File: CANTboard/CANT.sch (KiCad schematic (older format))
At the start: 24 parts, among them P1 SWD, P2 CAN, P3 USB, U1 STM32F042C6T6, U2 MCP2562-E/SN, U3 LD1117S33TR, U4 74LVC1G66

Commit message: Laid out CANT board based on STM32H7
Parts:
- removed C5, C6: 0.1uF, Capacitors_SMD:C_0805_HandSoldering, symbol pspice:C
- removed C7: 100nF, Capacitors_SMD:C_0805_HandSoldering, symbol pspice:C
- removed C8: 10uF, Capacitors_SMD:C_0805_HandSoldering, symbol pspice:C
- removed P2: CAN, Connectors_JST:JST_XH_S04B-XH-A_04x2.50mm_Angled, symbol Connector:Screw_Terminal_01x04
- removed U1: STM32F042C6T6, Housings_QFP:LQFP-48_7x7mm_Pitch0.5mm, symbol CANT-rescue:STM32F042C6T6-YaCANi
- removed U2: MCP2562-E/SN, Housings_SOIC:SOIC-8_3.9x4.9mm_Pitch1.27mm, symbol Interface_CAN_LIN:MCP2562-E-SN
- added C10, C9: 2.2uF, Capacitor_SMD:C_0805_2012Metric, symbol Device:C
- added C11, C12, C13: 100nF, Capacitor_SMD:C_0805_2012Metric, symbol pspice:C
- added C14: 100nF, Capacitor_SMD:C_0805_2012Metric, symbol Device:C_Small
- added C15: 1uF, Capacitor_SMD:C_0805_2012Metric, symbol Device:C_Small
- added C16, C17, C5, C6, C7: 100nF, Capacitor_SMD:C_0805_2012Metric, symbol Device:C
- added C8: 10uF, Capacitor_SMD:C_0805_2012Metric, symbol Device:C
- added D3: LED-RED, LED_SMD:LED_0805_2012Metric, symbol Device:LED
- added J1: Screw_Terminal_01x04, Connector_PinHeader_2.54mm:PinHeader_1x04_P2.54mm_Horizontal, symbol Connector:Screw_Terminal_01x04
- added JP3: Jumper_NC_Dual, Connector_PinHeader_2.54mm:PinHeader_1x03_P2.54mm_Vertical, symbol Device:Jumper_NC_Dual
- added R5, R7: 4.7K, Resistor_SMD:R_0805_2012Metric, symbol pspice:R
- added R6: 120, Resistor_SMD:R_0805_2012Metric, symbol pspice:R
- added R8: 68, Resistor_SMD:R_0805_2012Metric, symbol pspice:R
- added U1: STM32H743VITx, Package_QFP:LQFP-100_14x14mm_P0.5mm, symbol MCU_ST_STM32H7:STM32H743VITx
- added U2, U6: MCP2558FD-xSN, Package_SO:SOIC-8_3.9x4.9mm_P1.27mm, symbol Interface_CAN_LIN:MCP2558FD-xSN
- added U5: 74LVC1G66, Package_TO_SOT_SMD:SOT-353_SC-70-5_Handsoldering, symbol 74xGxx:74LVC1G66
- C1, C2, C4: value 0.1uF -> 100nF; footprint Capacitors_SMD:C_0805_HandSoldering -> Capacitor_SMD:C_0805_2012Metric
- C3: value 1uF -> 4.7uF; footprint Capacitors_SMD:C_0805_HandSoldering -> Capacitor_SMD:C_0805_2012Metric
- F1: footprint Capacitors_SMD:C_0805_HandSoldering -> Capacitor_SMD:C_0805_2012Metric
- JP1, JP2: footprint Pin_Headers:Pin_Header_Straight_1x03_Pitch2.54mm -> Connector_PinHeader_2.54mm:PinHeader_1x03_P2.54mm_Vertical
- P1: footprint Pin_Headers:Pin_Header_Straight_1x05_Pitch2.54mm -> Connector_PinHeader_2.54mm:PinHeader_1x05_P2.54mm_Vertical
- P3: footprint Connectors_Molex:USB_Micro-B_Molex_47346-0001 -> Connector_USB:USB_Micro-B_Molex_47346-0001
- R1, R2: footprint Resistors_SMD:R_0805_HandSoldering -> Resistor_SMD:R_0805_2012Metric
- R3, R4: value R -> 68; footprint Resistors_SMD:R_0805_HandSoldering -> Resistor_SMD:R_0805_2012Metric
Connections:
- net labels added: CAN1_H, CAN1_L, CAN1_RX, CAN1_SHORT, CAN1_TX, CAN2_H, CAN2_L, CAN2_RX, CAN2_SHORT, CAN2_TX, LED_ACT1, LED_ACT2, LED_PWR1
- net labels removed: CAN_H, CAN_L, CAN_RX, CAN_SHORT, CAN_TX, LED_ACT, LED_PWR
- wire segments 54 -> 86
- no-connect marks 32 -> 73
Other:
- moved on the sheet: C1, C2, C3, C4, D1, D2, F1, JP1, JP2, P1, P3, R1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

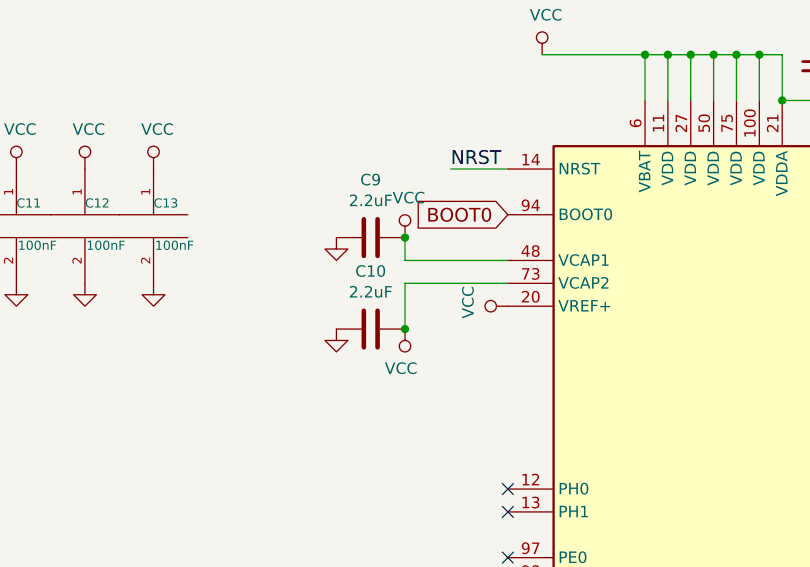
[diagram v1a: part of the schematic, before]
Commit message: Fix VCAP connection issue - apparently, these are not supposed to be connected to VDD
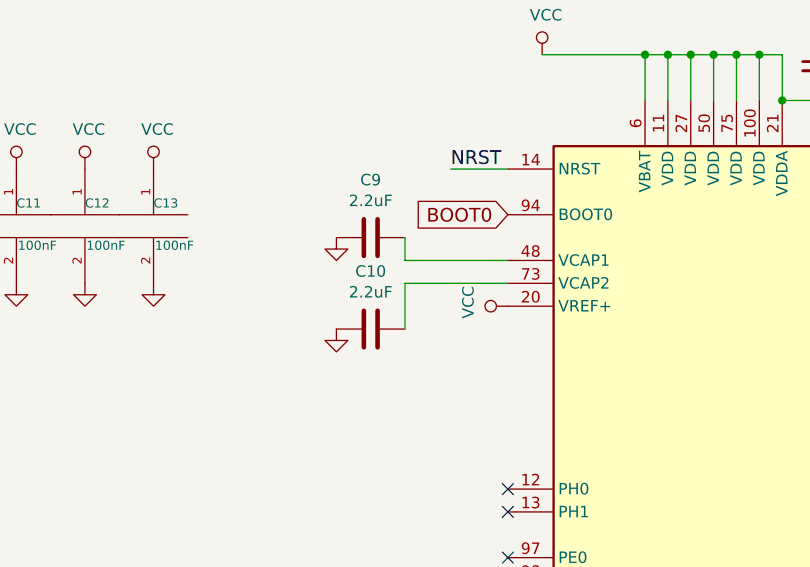
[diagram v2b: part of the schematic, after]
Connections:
- net VCC: no longer C10.1, C9.1, U1.48 (VCAP1), U1.73 (VCAP2)
- new net: C9.1, U1.48 (VCAP1)
- new net: C10.1, U1.73 (VCAP2)
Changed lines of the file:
@@
 	1    0    0    -1
-$EndComp
-$Comp
-L Device:C C9
-U 1 1 5CDF6F1D
-P 3650 1550
-F 0 "C9" V 3398 1550 50  0000 C CNN
-F 1 "2.2uF" V 3489 1550 50  0000 C CNN
-F 2 "Capacitor_SMD:C_0805_2012Metric" H 3688 1400 50  0001 C CNN
-F 3 "~" H 3650 1550 50  0001 C CNN
-	1    3650 1550
-	0    1    1    0
 $EndComp
 Wire Wire Line
@@
 Wire Wire Line
 	3800 1750 3800 1950
-Connection ~ 3800 1550
 $Comp
 L Device:C C10
@@
 	0    1    1    0
 $EndComp
-$Comp
-L power:VCC #PWR0116
-U 1 1 5D0945AE
-P 3800 1550
-F 0 "#PWR0116" H 3800 1400 50  0001 C CNN
-F 1 "VCC" H 3817 1723 50  0000 C CNN
-F 2 "" H 3800 1550 50  0001 C CNN
-F 3 "" H 3800 1550 50  0001 C CNN
-	1    3800 1550
-	1    0    0    -1
-$EndComp
-$Comp
-L power:VCC #PWR0117
-U 1 1 5D098145
-P 3800 1950
-F 0 "#PWR0117" H 3800 1800 50  0001 C CNN
-F 1 "VCC" H 3817 2123 50  0000 C CNN
-F 2 "" H 3800 1950 50  0001 C CNN
-F 3 "" H 3800 1950 50  0001 C CNN
-	1    3800 1950
-	-1   0    0    1
-$EndComp
-Connection ~ 3800 1950
 $Comp
 L Device:C C17
@@
 LED_ACT2
 NoConn ~ 6050 3250
+$Comp
+L Device:C C9
+U 1 1 5CDF6F1D
+P 3650 1550
+F 0 "C9" V 3398 1550 50  0000 C CNN
+F 1 "2.2uF" V 3489 1550 50  0000 C CNN
+F 2 "Capacitor_SMD:C_0805_2012Metric" H 3688 1400 50  0001 C CNN
+F 3 "~" H 3650 1550 50  0001 C CNN
+	1    3650 1550
+	0    1    1    0
+$EndComp
 $EndSCHEMATC
